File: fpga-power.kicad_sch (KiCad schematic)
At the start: 111 parts, among them U34 XCAU25P-2FFVB676I

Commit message: [#66311] Replace HyperRam and Flash with 1V8 parts. Add 1V25 ADC VREF for core temp measurement (internal)
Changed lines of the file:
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@@
+    (stroke (width 0) (type default))
+  )
+  (wire (pts (xy 231.775 161.29) (xy 240.03 161.29))
     (stroke (width 0) (type default))
   )
@@
     (stroke (width 0) (type default))
   )
-  (wire (pts (xy 240.03 161.29) (xy 231.775 161.29))
-    (stroke (width 0) (type default))
-  )
   (polyline (pts (xy 139.065 58.42) (xy 157.48 58.42))
     (stroke (width 0) (type dash))
@@
     (stroke (width 0) (type default))
   )
-  (wire (pts (xy 231.775 166.37) (xy 231.775 161.29))
-    (stroke (width 0) (type default))
-  )
   (wire (pts (xy 330.835 87.63) (xy 330.835 89.535))
     (stroke (width 0) (type default))
@@
     (stroke (width 0) (type default))
   )
+  (wire (pts (xy 231.775 161.29) (xy 231.775 166.37))
+    (stroke (width 0) (type default))
+  )
   (wire (pts (xy 184.785 94.615) (xy 184.785 93.345))
     (stroke (width 0) (type default))
@@
     (stroke (width 0) (type default))
   )
-  (wire (pts (xy 231.775 161.29) (xy 231.775 151.13))
-    (stroke (width 0) (type default))
-  )
+  (wire (pts (xy 231.775 151.13) (xy 231.775 161.29))
+    (stroke (width 0) (type default))
+  )

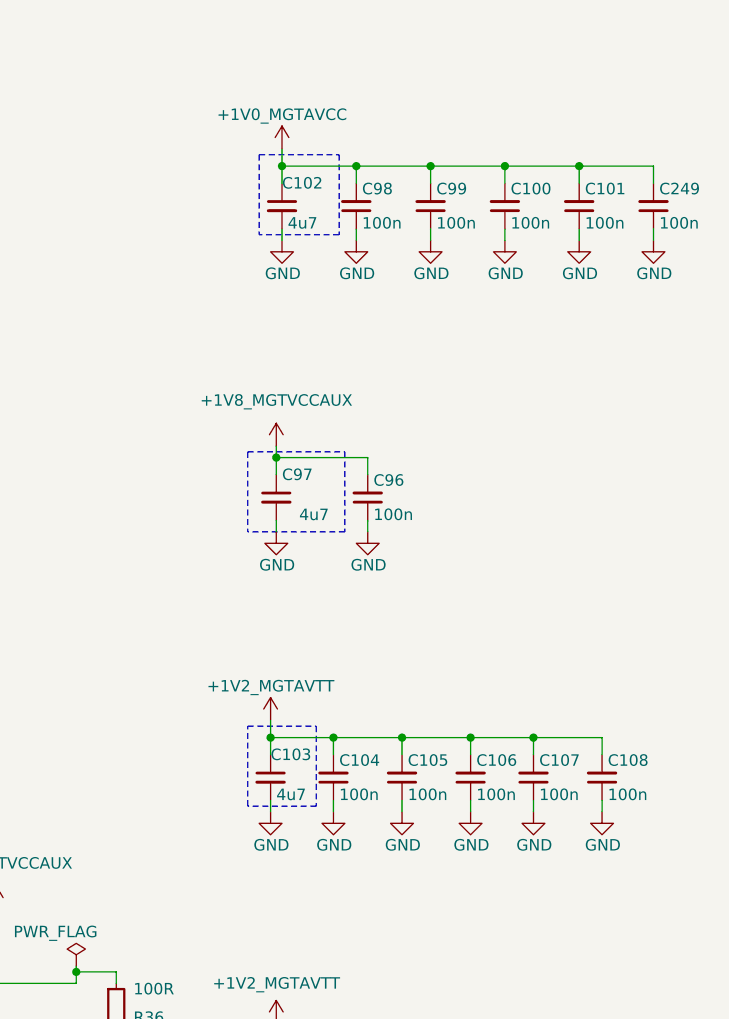
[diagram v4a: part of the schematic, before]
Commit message: [#66300] Replace MGTACC and MGTAVTT high side current measurement resistor, optimize decoupling
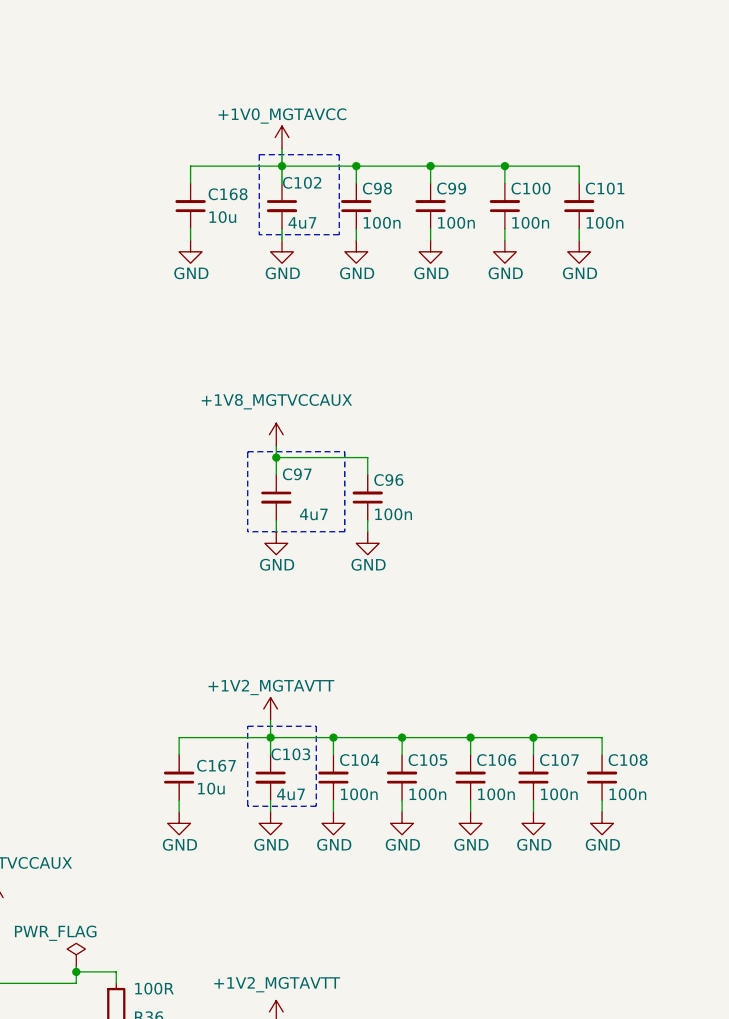
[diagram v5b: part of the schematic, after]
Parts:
- removed C249: C_100n_0402, antmicro-footprints:C_0402_1005Metric, symbol antmicroCapacitors0402:C_100n_0402
- added C167, C168: C_10u_10V_0402, antmicro-footprints:C_0402_1005Metric, symbol antmicroCapacitors0402:C_10u_10V_0402
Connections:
- net +1V0_MGTAVCC: now also C168.2
- net +1V2_MGTAVTT: now also C167.2
- net GND: now also C167.1, C168.1

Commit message: [#67115] Place decoupling under FPGA
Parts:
- removed C15, C69: C_47u_0603, antmicro-footprints:C_0603_1608Metric, symbol antmicroCapacitors0603:C_47u_0603
- removed C21, C244, C245, C28, C29, C31, C63, C66, C70, C72, C77, C81, C82, C93: C_100n_0402, antmicro-footprints:C_0402_1005Metric, symbol antmicroCapacitors0402:C_100n_0402
- removed C80, C83: C_1u_25V_0402, antmicro-footprints:C_0402_1005Metric, symbol antmicroCapacitors0402:C_1u_25V_0402
- added C15, C310, C311, C312, C80, C83: C_100n_0402, antmicro-footprints:C_0402_1005Metric_EIA, symbol antmicroCapacitors0402:C_100n_0402
- added C31, C63: C_47u_0603, antmicro-footprints:C_0603_1608Metric, symbol antmicroCapacitors0603:C_47u_0603
- added C66: C_Pol_1m_2.5V_KEMET-T520-D, antmicro-footprints:C_Pol_EIA-D, symbol antmicroCapacitorspol:C_Pol_1m_2.5V_KEMET-T520-D
- added C70: C_10u_10V_0402, antmicro-footprints:C_0402_1005Metric_EIA, symbol antmicroCapacitors0402:C_10u_10V_0402
- added C72: C_4u7_0402, antmicro-footprints:C_0402_1005Metric_EIA, symbol antmicroCapacitors0402:C_4u7_0402
- added C77, C81: C_1u_25V_0402, antmicro-footprints:C_0402_1005Metric_EIA, symbol antmicroCapacitors0402:C_1u_25V_0402
- C100, C101, C102, C103, C104, C105, C106, C107, C108, C13, C16, C167, C168, C17, C18, C19, C20, C23, C24, C243, C246, C247, C248, C26, C30, C33, C34, C35, C36, C37, C39, C40, C41, C42, C43, C45, C46, C47, C48, C49, C50, C51, C52, C53, C55, C56, C57, C58, C59, C60, C61, C64, C65, C67, C68, C71, C74, C75, C76, C78, C79, C84, C86, C87, C88, C89, C90, C91, C92, C95, C96, C97, C98, C99: footprint antmicro-footprints:C_0402_1005Metric -> antmicro-footprints:C_0402_1005Metric_EIA
- R36: footprint antmicro-footprints:R_0402_1005Metric -> antmicro-footprints:R_0402_1005Metric_EIA
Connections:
- net +0V85: now also C246.2, C247.2, C248.2, C34.2, C35.2, C36.2, C39.2, C40.2, C41.2, C43.2, C45.2, C46.2, C47.2, C50.2, C51.2, C52.2, C53.2, C56.2, C57.2, C58.2, C59.2, C64.2, C75.2, C79.2, C84.2, C86.2, C88.2, C90.2, C92.2, C66.1
- net +1V0_MGTAVCC: now also C63.1
- net +1V1: no longer C14.1, C85.1, C87.2, C89.2, C91.2
- net +1V2_MGTAVTT: now also C14.1, C310.2, C311.2, C312.2, C70.2, C72.1, C80.2, C83.2
- net +1V8: now also C85.1, C87.2, C89.2, C91.2, C15.2, C77.2, C81.2; no longer C64.2
- net +1V8_MGTVCCAUX: now also C31.1
- net GND: now also C15.1, C31.2, C310.1, C311.1, C312.1, C63.2, C66.2, C70.1, C72.2, C77.1, C80.1, C81.1, C83.1
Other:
- moved on the sheet: C76

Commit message: [#67532] Clean DRC. Optimize power planes, EMC concept and LS/HS routing
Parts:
- C27: footprint antmicro-footprints:C_0402_1005Metric -> antmicro-footprints:C_0402_1005Metric_EIA
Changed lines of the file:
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@@
       (effects (font (size 1.27 1.27) (thickness 0.15)) (justify left bottom) hide)
     )
-    (property "Footprint" "antmicro-footprints:C_0402_1005Metric" (at 57.15 101.6 0)
+    (property "Footprint" "antmicro-footprints:C_0402_1005Metric_EIA" (at 57.15 101.6 0)
       (effects (font (size 1.27 1.27) (thickness 0.15)) (justify left bottom) hide)
     )

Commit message: [#67725] Clean-up fpga-power sheet
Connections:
- net +1V8 is gone; now on net +0V85: C11.1, C15.2, C18.2, C27.2, C30.2, C68.2, C73.1, C76.2, C77.2, C81.2, C85.1, C87.2, C89.2, C91.2, U34.M18 (VCCAUX), U34.N14 (VCCADC), U34.N18 (VCCAUX), U34.P18 (VCCAUX_IO), U34.R18 (VCCAUX_IO), U34.T18 (VCCAUX_IO), U34.Y9 (VBATT)
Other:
- note added: "Bank decoupling"
- note added: "Bank marked by dashed line referenced from US+ Series FPGAs PCB Design Guide UG583 (AUP25P+ XCKU5P FFVB Package worst case)"
- note added: "FPGA"
- note added: "MGT decoupling"
- note added: "VCCINT decoupling"
- note removed: "Bank marked by dahed line referenced from US+ Series FPGAs PCB Design Guide UG583 (AUP25P+ XCKU5P FFVB Package worst case)"
- moved on the sheet: C100, C101, C102, C103, C104, C105, C106, C107, C108, C11, C12, C13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
